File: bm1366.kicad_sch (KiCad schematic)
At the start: 54 parts, among them J3 Conn_01x05, U1 25MHz, U14 BM1366_mode1, U2 TXB0104RGYR, U5 MCP1824T-1802E, U6 MCP1824T-0802E

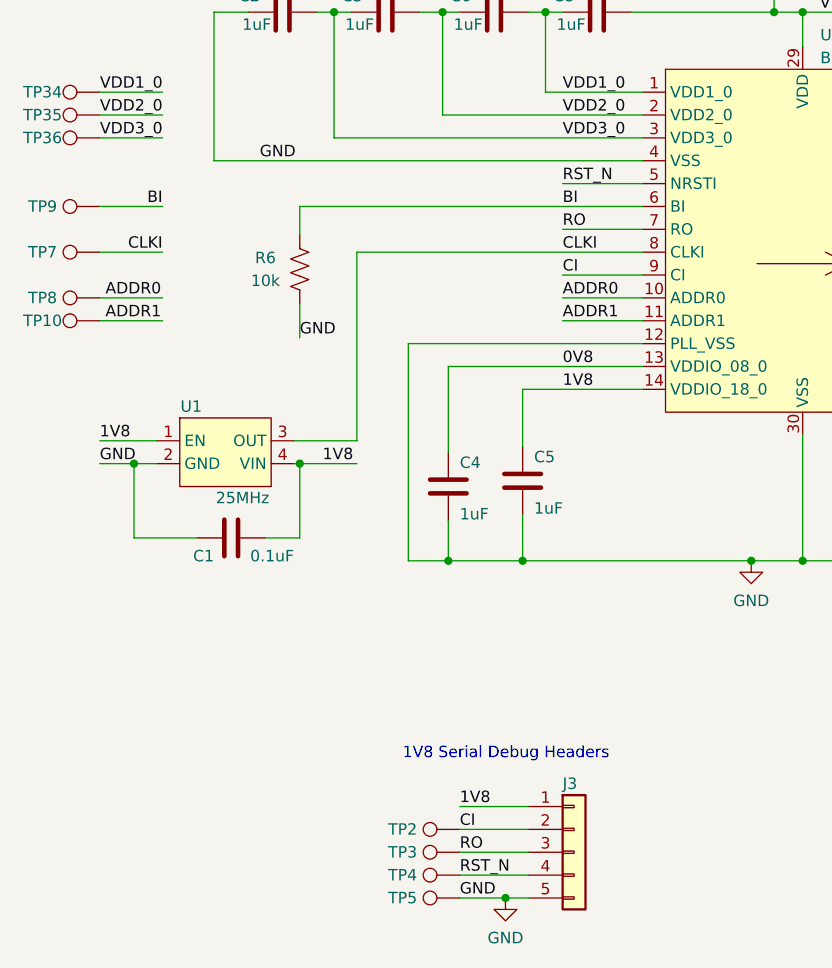
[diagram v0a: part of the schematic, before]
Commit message: Power analysis; updates to 205pd
Started analysis based on the 204 with an architecture diagram and with an smath document. Copied over manually changes from the 205 branch and started updating the schematic with USB PD capabilities. Only added decoy USB PD chip (CH224K), still need to fix power supplies.
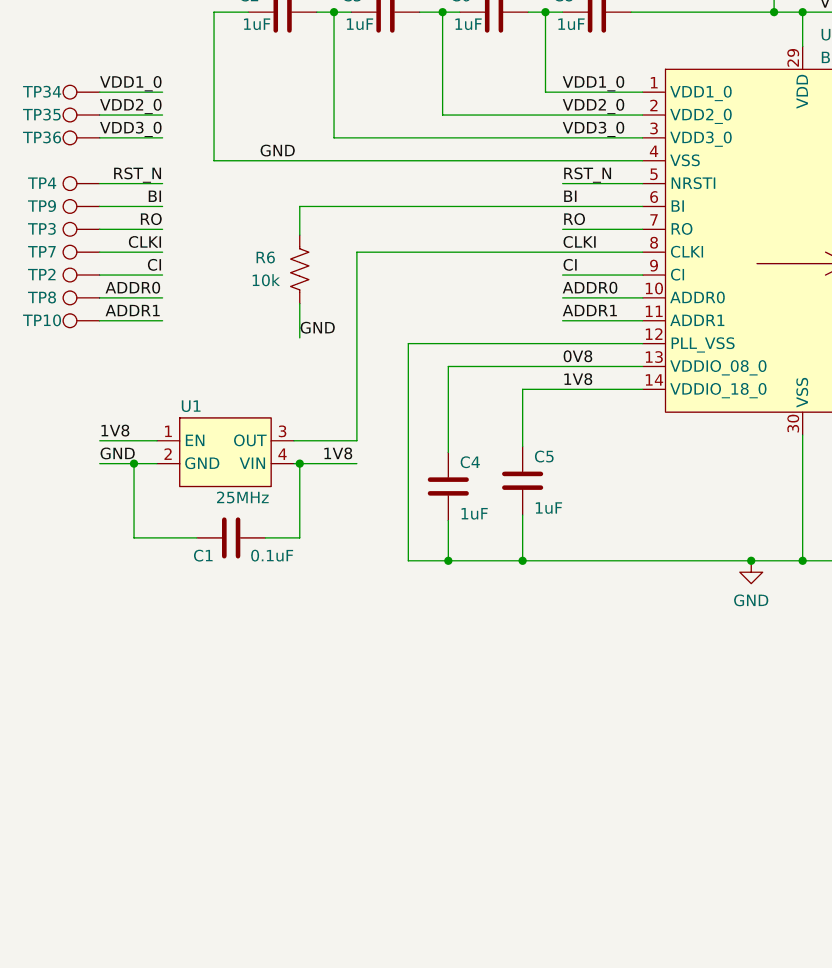
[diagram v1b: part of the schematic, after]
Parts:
- removed J3: Conn_01x05, Connector_PinHeader_2.54mm:PinHeader_1x05_P2.54mm_Vertical, symbol Connector_Generic:Conn_01x05
- removed TP5: TestPoint, TestPoint:TestPoint_Pad_D1.5mm, symbol Connector:TestPoint
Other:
- note removed: "1V8 Serial Debug Headers"

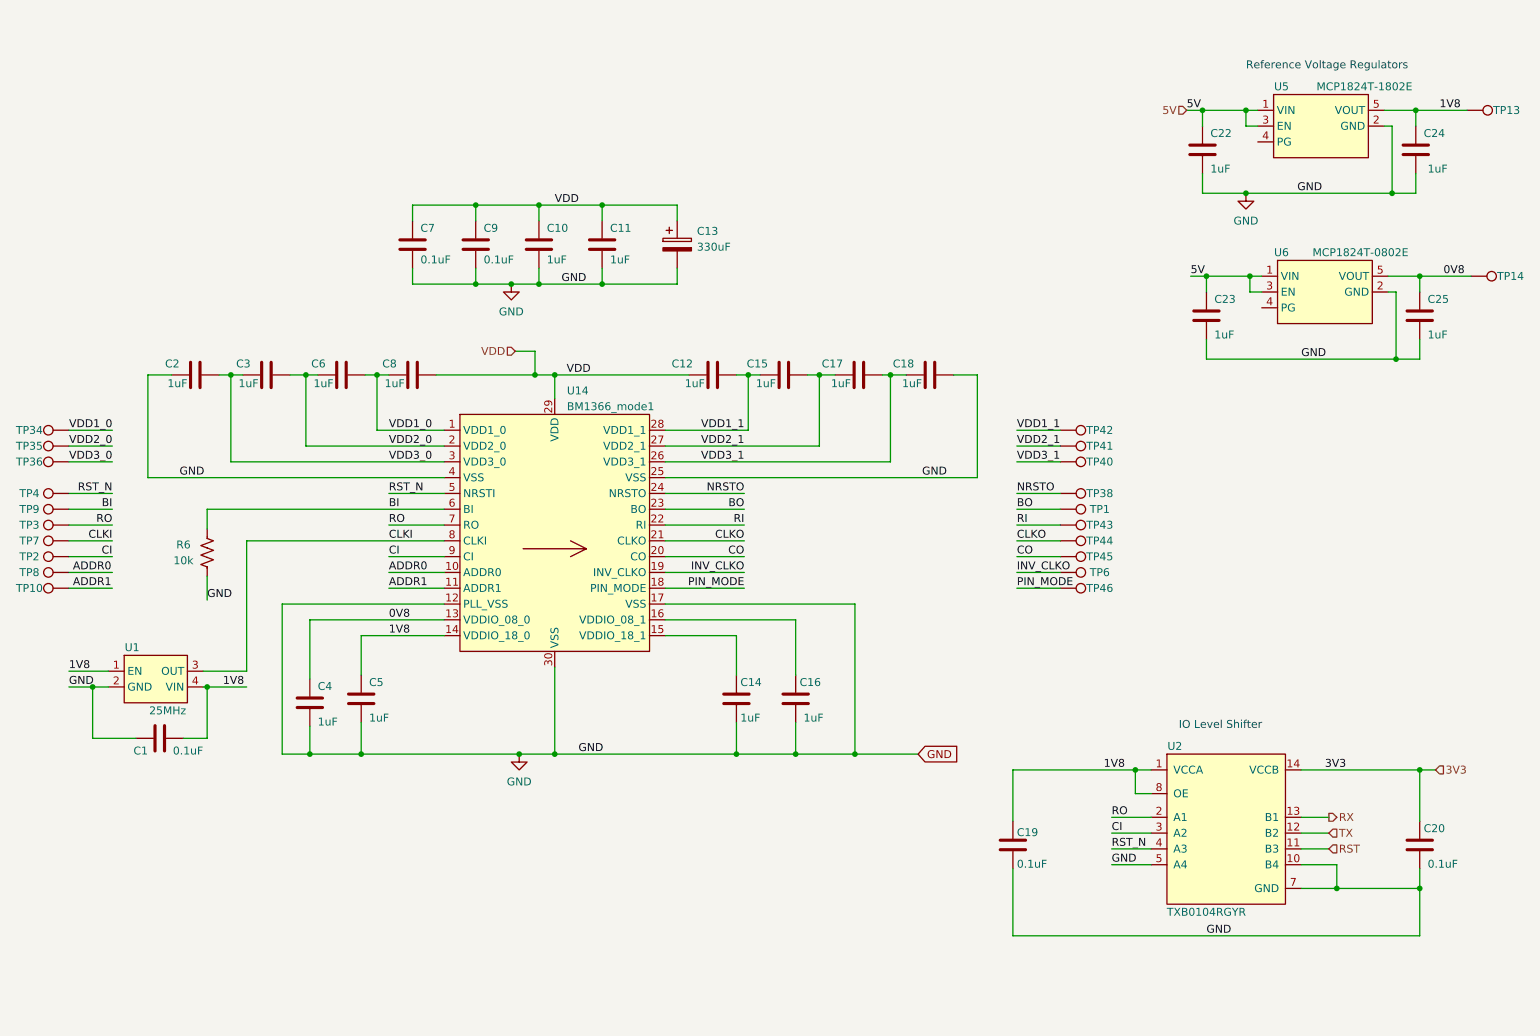
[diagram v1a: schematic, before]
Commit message: Worked on VDD
Started importing SiC431A for VDD supply. Yet to do Vfb, Mode, Pgood, boot, phase, en. Moved power supplies to power page. Configured CH224K to 12V
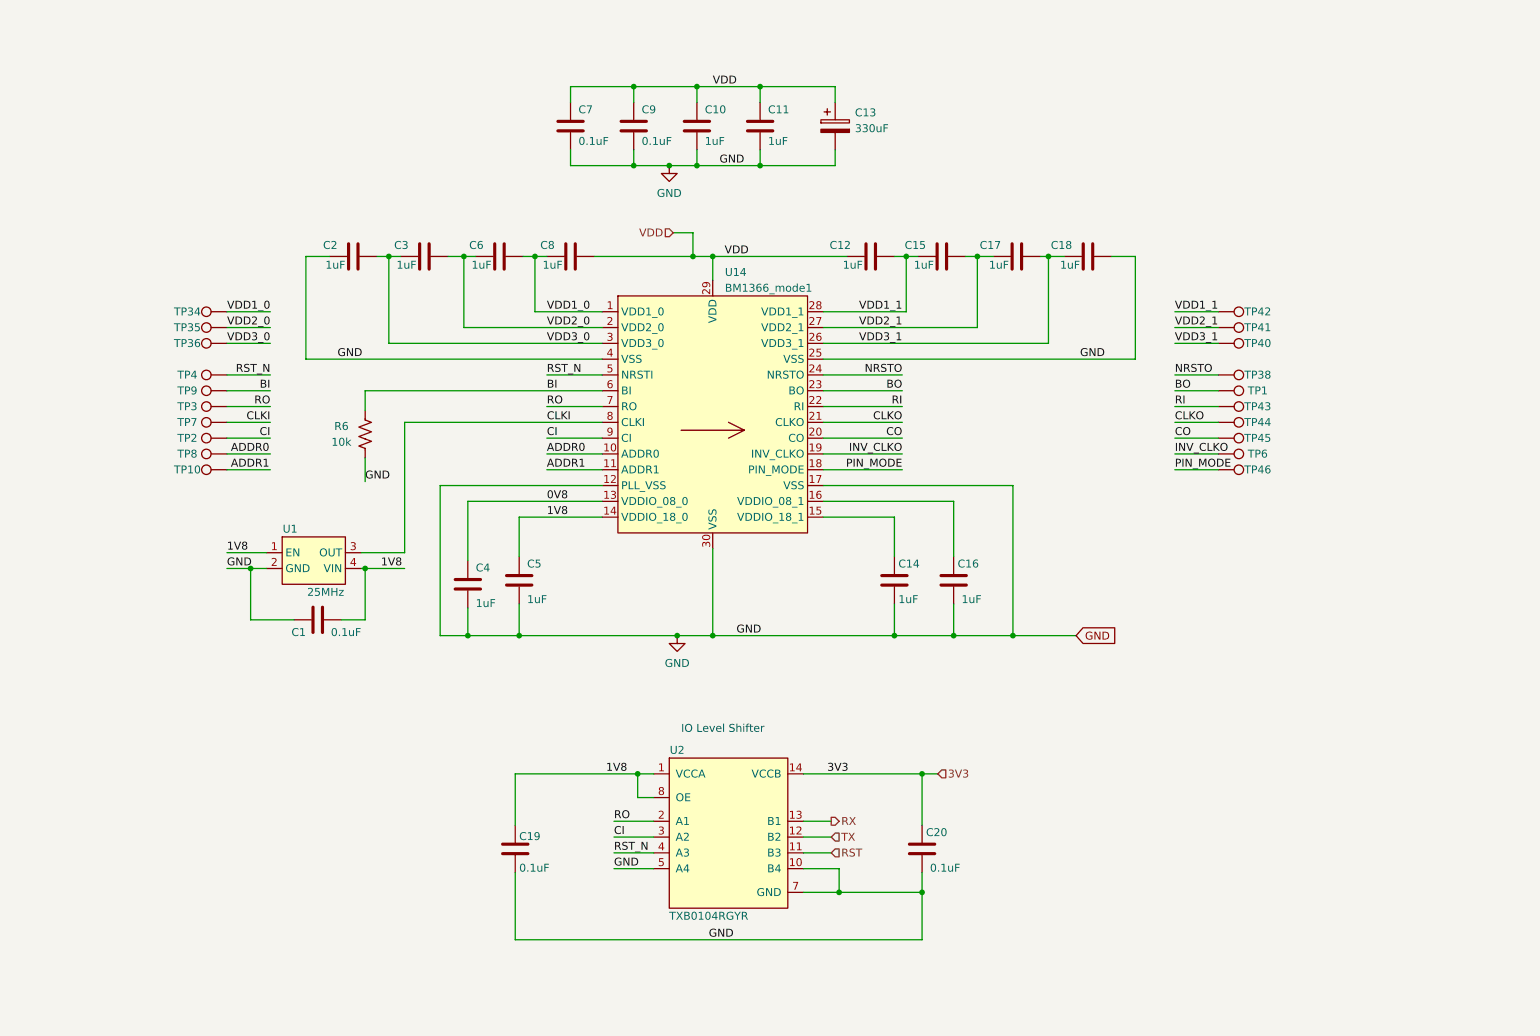
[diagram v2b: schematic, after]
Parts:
- removed C22, C23, C24, C25: 1uF, Capacitor_SMD:C_0402_1005Metric, symbol Device:C
- removed TP13, TP14: TestPoint, TestPoint:TestPoint_Pad_D1.5mm, symbol Connector:TestPoint
- removed U5: MCP1824T-1802E, Package_TO_SOT_SMD:SOT-23-5, symbol bitaxe:MCP1824
- removed U6: MCP1824T-0802E, Package_TO_SOT_SMD:SOT-23-5, symbol bitaxe:MCP1824
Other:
- note removed: "Reference Voltage Regulators"
- moved on the sheet: C1, C10, C11, C12, C13, C14, C15, C16, C17, C18, C19, C2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

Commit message: SCH Draft 3, PCB Start
Finished some last minute changes to change 1V8 to 1V2 based on discord feedback. Updated level shifter and moved 25MHz oscillator to use 3V3 and be shifted down. Started working on layout.
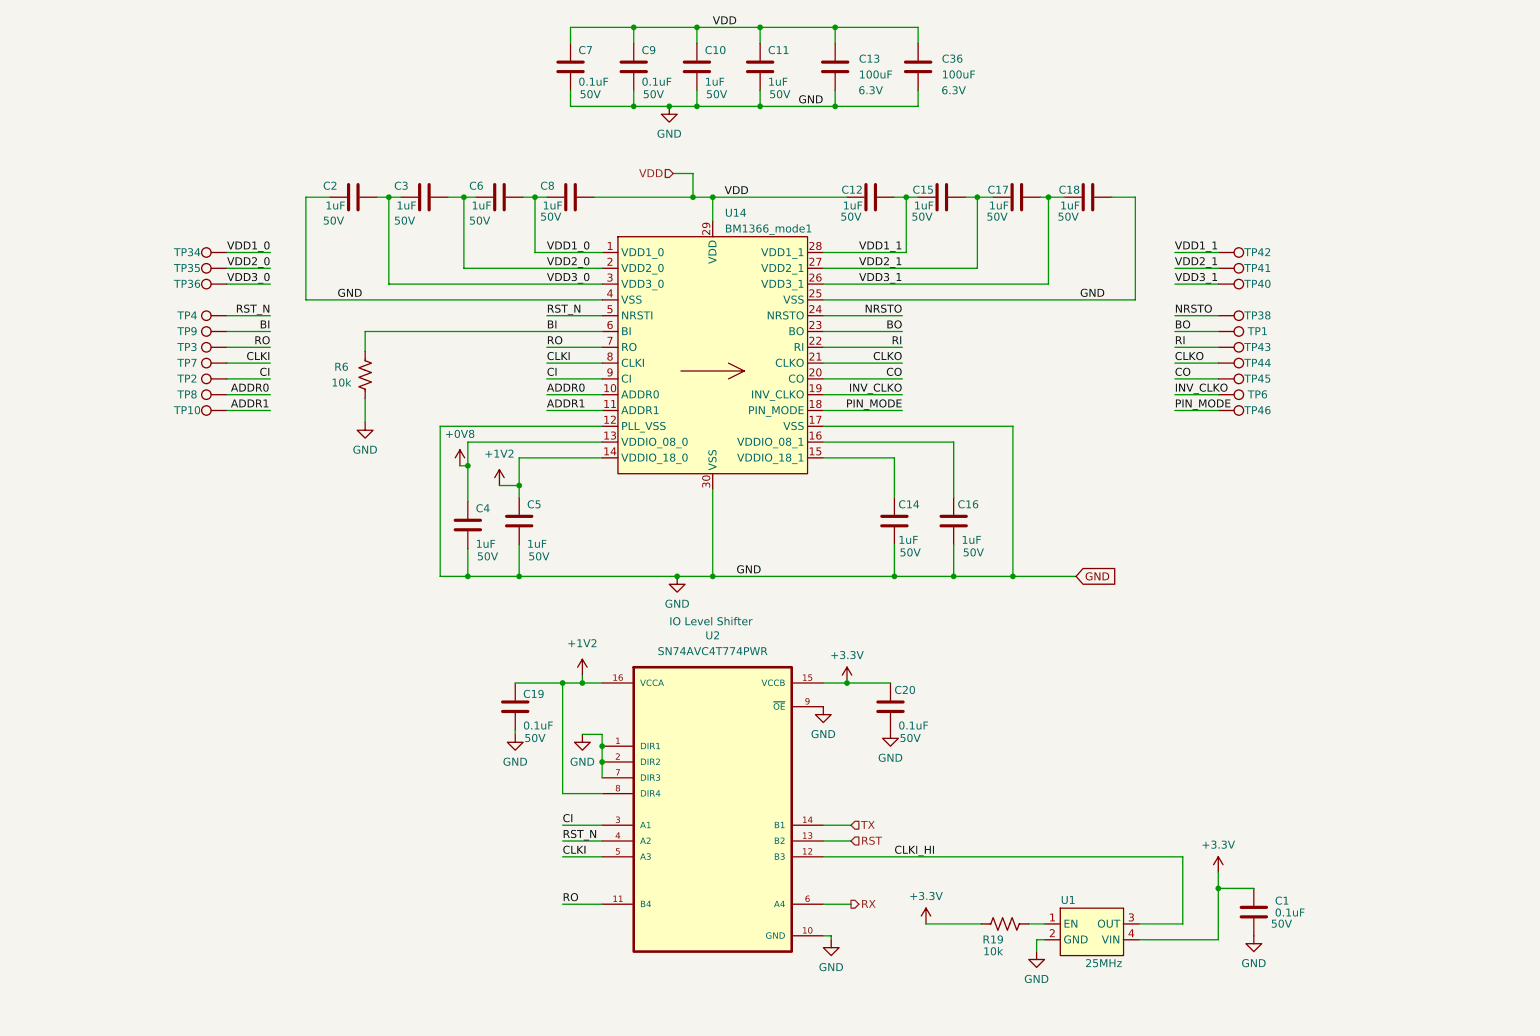
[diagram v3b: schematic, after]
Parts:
- removed C13: 330uF, Capacitor_Tantalum_SMD:CP_EIA-7343-31_Kemet-D_Pad2.25x2.55mm_HandSolder, symbol Device:C_Polarized
- removed U2: TXB0104RGYR, bitaxe:TXB0104, symbol bitaxe:TXB0104RGYR
- added C13, C36: 100uF, Capacitor_SMD:C_1206_3216Metric, symbol Device:C
- added R19: 10k, Resistor_SMD:R_0402_1005Metric, symbol Device:R_US
- added U2: SN74AVC4T774PWR, bitaxe:SOP65P640X120-16N, symbol bitaxe:SN74AVC4T774PWR
- C1, C19, C20, C7, C9: DK 1292-1639-1-ND -> 490-13342-1-ND; PARTNO 0402X104K100CT -> GRM155R71H104KE14J; Voltage (none) -> 50V
- C10, C11, C12, C14, C15, C16, C17, C18, C2, C3, C4, C5, C6, C8: footprint Capacitor_SMD:C_0402_1005Metric -> Capacitor_SMD:C_0603_1608Metric; DK 587-5514-1-ND -> 311-2082-1-ND; PARTNO EMK105BJ105MV-F -> CC0603KRX7R9BB105; Voltage (none) -> 50V
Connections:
- net CI: now also U2.3 (A1)
- net CLKI: now also U2.5 (A3); no longer U1.3 (OUT)
- net GND: now also C13.2, C36.2, U2.1 (DIR1), U2.10 (GND), U2.2 (DIR2), U2.7 (DIR3), U2.9 (~{OE})
- net RO: now also U2.11 (B4)
- net RST: now also U2.13 (B2)
- net RST_N: now also U2.4 (A2)
- net RX: now also U2.6 (A4)
- net TX: now also U2.14 (B1)
- net VDD: now also C13.1, C36.1
- net 0V8 renamed +0V8
- net 1V8 renamed +1V2
- net +1V2: now also U2.16 (VCCA), U2.8 (DIR4); no longer C1.2, U1.1 (EN), U1.4 (VIN)
- net 3V3 renamed +3.3V
- net +3.3V: now also C1.2, U1.4 (VIN), R19.2, U2.15 (VCCB)
- new net: R19.1, U1.1 (EN)
- new net CLKI_HI: U1.3 (OUT), U2.12 (B3)
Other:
- moved on the sheet: C10, C11, C12, C14, C15, C16, C17, C18, C2, C3, C4, C5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
